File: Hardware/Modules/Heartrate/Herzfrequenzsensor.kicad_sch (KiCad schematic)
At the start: 8 parts, among them U1 MAX30101EFD_T, U2 TLV70018_SOT23-5, U4 PCA9306DCTR

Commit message: HeartRateV2
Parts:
- removed C3, C4: 1µ, Capacitor_SMD:C_0603_1608Metric_Pad1.08x0.95mm_HandSolder, symbol Device:C
- removed J1, J2: ~, Connector_JST:JST_EH_B4B-EH-A_1x04_P2.50mm_Vertical, symbol Modular_Electronics_Toolkit:CONN_I2C
- removed R1: 200k, Resistor_SMD:R_0603_1608Metric_Pad0.98x0.95mm_HandSolder, symbol Device:R
- removed U1: MAX30101EFD_T, Modular_Electronics_Toolkit:PSON80P560X330X165-14N, symbol Modular_Electronics_Toolkit:MAX30101EFD_T
- removed U2: TLV70018_SOT23-5, Package_TO_SOT_SMD:SOT-23-5, symbol Regulator_Linear:TLV70018_SOT23-5
- removed U4: PCA9306DCTR, Modular_Electronics_Toolkit:SOP65P400X130-8N, symbol Modular_Electronics_Toolkit:PCA9306DCTR
- added C10: 0.1µF, Capacitor_SMD:C_0603_1608Metric_Pad1.08x0.95mm_HandSolder, symbol Device:C
- added C11, C12: 4.7µF, Capacitor_SMD:C_0603_1608Metric_Pad1.08x0.95mm_HandSolder, symbol Device:C
- added C6, C7, C8, C9: 1µ, Capacitor_SMD:C_0603_1608Metric_Pad1.08x0.95mm_HandSolder, symbol Device:C
- added J4, J5: B4B-EH-A, Connector_JST:JST_EH_B4B-EH-A_1x04_P2.50mm_Vertical, symbol Modular_Electronics_Toolkit_sym:B4B-EH-A
- added J6: Conn_01x01_Pin, Connector_PinHeader_2.54mm:PinHeader_1x01_P2.54mm_Vertical, symbol Connector:Conn_01x01_Pin
- added R3: 200k, Resistor_SMD:R_0603_1608Metric_Pad0.98x0.95mm_HandSolder, symbol Device:R
- added R4, R5, R6, R7: 4.7k, Resistor_SMD:R_0603_1608Metric_Pad0.98x0.95mm_HandSolder, symbol Device:R
- added R8: 10R, Resistor_SMD:R_0603_1608Metric_Pad0.98x0.95mm_HandSolder, symbol Device:R
- added U6: MAX30101EFD_T, Modular_Electronics_Toolkit:PSON80P560X330X165-14N, symbol Modular_Electronics_Toolkit:MAX30101EFD_T
- added U7: PCA9306DCTR, Modular_Electronics_Toolkit:SOP65P400X130-8N, symbol Modular_Electronics_Toolkit:PCA9306DCTR
- added U8: MAX32664GTGA_T, Modular_Electronics_Toolkit:IC_MAX32664GTGA_T, symbol Modular_Electronics_Toolkit_sym:MAX32664GTGA_T
- added U9: TLV70018_SOT23-5, Package_TO_SOT_SMD:SOT-23-5, symbol Regulator_Linear:TLV70018_SOT23-5
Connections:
- net GND: now also C11.2, C12.2, C6.1, C7.1, C8.2, C9.2, J4.4, J5.4, R8.2, U6.12 (GND), U6.4 (PGND), U7.1 (GND), U8.10 (VSS__1), U8.7 (VSS), U9.2 (GND)
- new net: C6.2, U8.12 (VCORE)
- new net: C10.1, R8.1
- new net: R3.1, U7.7 (VREF2), U7.8 (EN)
- new net: C10.2, U8.6 (~{RST})
- new net B1: R4.1, U7.4 (SDA1), U8.23 (SLAVE_SDA)
- new net B2: R5.1, U7.3 (SCL1), U8.24 (SLAVE_SCL)
- new net B3: R6.1, U6.3 (SDA), U8.13 (SENSOR_SDA)
- new net B4: R7.1, U6.2 (SCL), U8.14 (SENSOR_SCL)
- new net INT: U6.13 (~{INT}), U8.18 (HR_INT)
- new net J1: J6.1 (Pin_1), U8.1 (MFIO)
- new net SCL: J4.2, J5.2, U7.6 (SCL2)
- new net SDA: J4.3, J5.3, U7.5 (SDA2)
- new net VCC: C11.1, C8.1, J4.1, J5.1, R3.2, U6.10 (VLED+__1), U6.9 (VLED+), U9.1 (IN)
- new net VDD__1: C7.2, C9.1, R4.2, R5.2, R6.2, R7.2, U8.11 (VDD), U8.22 (VDD__1), U9.5 (OUT)
- new net VREF: C12.1, U6.11 (VDD), U7.2 (VREF1)
- no-connect marks 0 -> 4

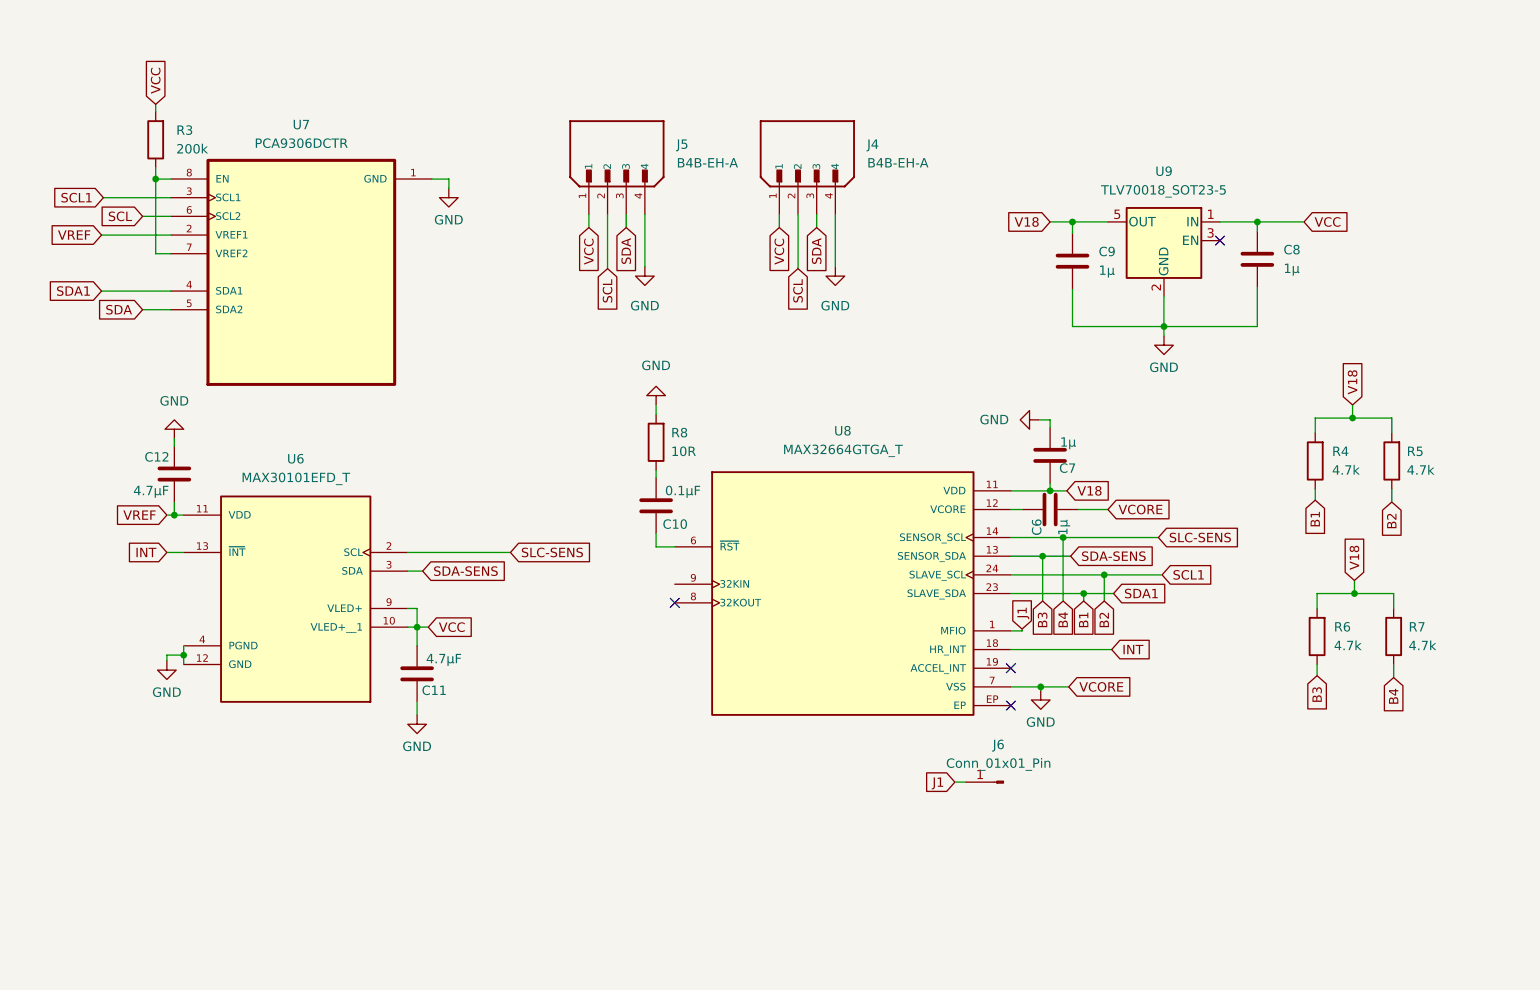
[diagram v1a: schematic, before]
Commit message: Finishing Modules
Wifi-Module
Flight-Module
REPAIR:
- Heartrate
- Flight-Module
- Wifi-Module
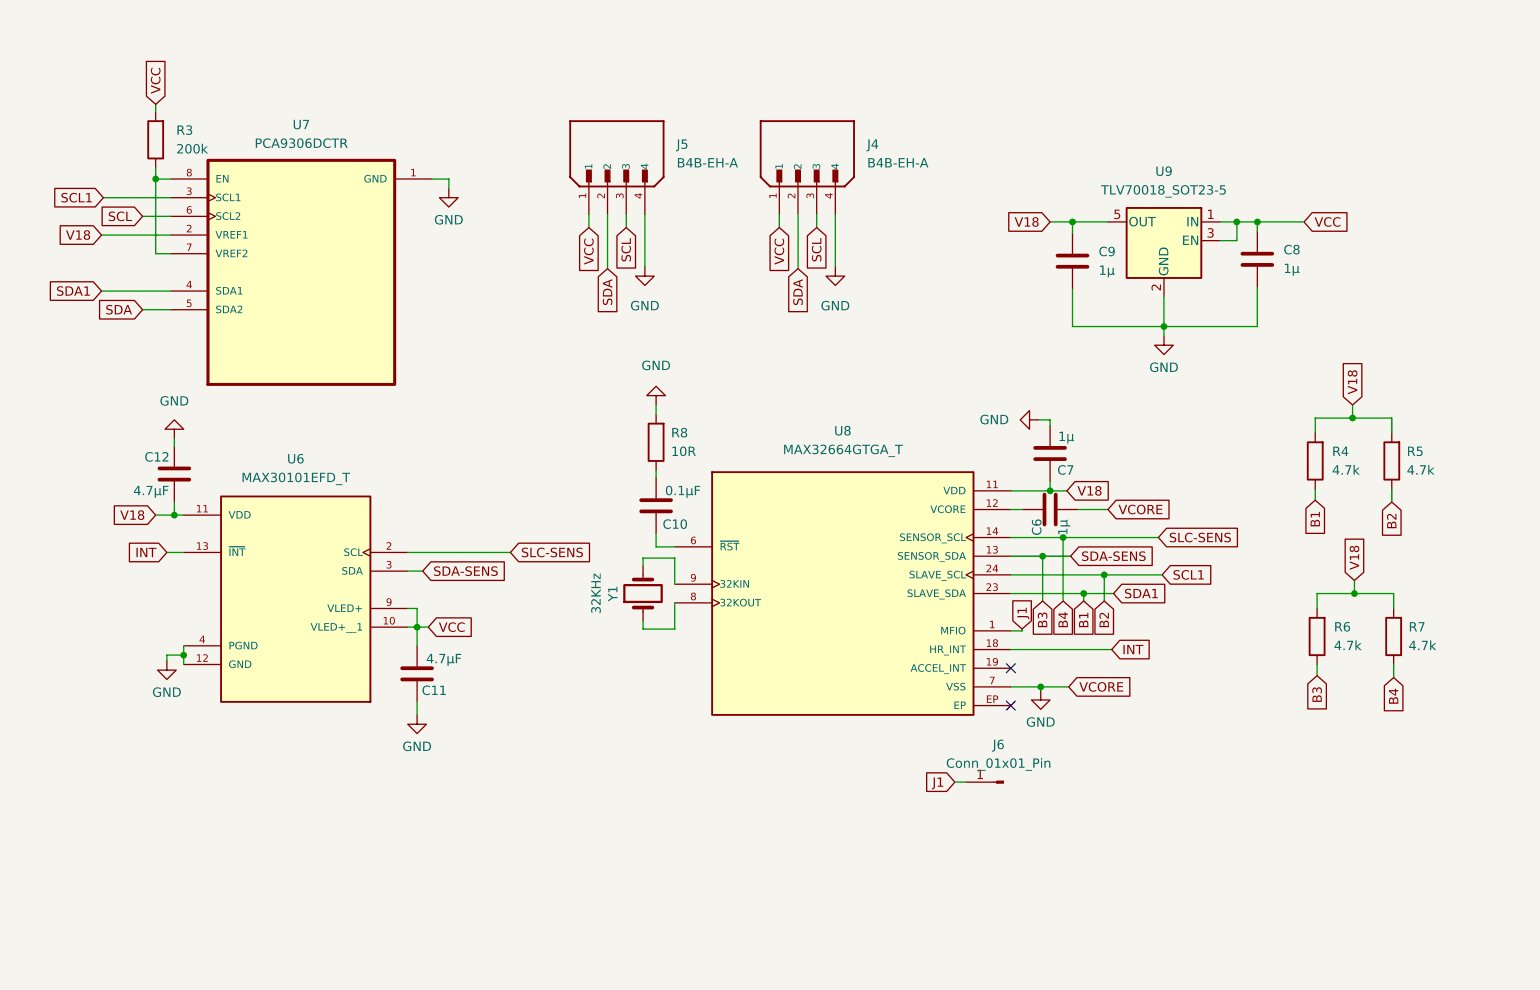
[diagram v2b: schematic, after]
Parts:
- added Y1: 32KHz, Modular-Electronics-Toolkit-BP:XTAL_CM7V-T1A-LOW-ESR-32.768KHZ-6PF-20-TA-QC, symbol Device:Crystal
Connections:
- net VREF is gone; now on net VDD__1: C12.1, U6.11 (VDD), U7.2 (VREF1)
- net SCL: now also J4.3, J5.3; no longer J4.2, J5.2
- net SDA: now also J4.2, J5.2; no longer J4.3, J5.3
- net VCC: now also U9.3 (EN)
- net at U8.8 (32KOUT): now also Y1.1
- net at U8.9 (32KIN): now also Y1.2
- no-connect marks 4 -> 2

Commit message: Pushing Final Versions of all Modules (2025)
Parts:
- Y1: footprint Modular-Electronics-Toolkit-BP:XTAL_CM7V-T1A-LOW-ESR-32.768KHZ-6PF-20-TA-QC -> Modular-Elektronics-Toolkit-Global-Libary:XTAL_CM7V-T1A-LOW-ESR-32.768KHZ-6PF-20-TA-QC
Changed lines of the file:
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@@
 (kicad_sch
-	(version 20231120)
+	(version 20250114)
 	(generator "eeschema")
-	(generator_version "8.0")
+	(generator_version "9.0")
 	(paper "A4")
 	(junction
@@
 	)
 	(junction
-		(at 162.052 107.188)
-		(diameter 0)
-		(color 0 0 0 0)
-	)
-	(junction
 		(at 45.466 102.87)
 		(diameter 0)
@@
 	(wire
 		(pts
-			(xy 162.052 107.188) (xy 165.862 107.188)
-		)
-		(stroke
-			(width 0)
-			(type default)
-		)
-	)
-	(wire
-		(pts
 			(xy 178.816 58.166) (xy 191.516 58.166)
 		)
@@
 		)
 	)
-	(global_label "VCORE"
-		(shape input)
-		(at 171.196 83.058 0)
-		(fields_autoplaced yes)
-		(effects
-			(font
-				(size 1.27 1.27)
-			)
-			(justify left)
-		)
-		(property "Intersheetrefs" "${INTERSHEET_REFS}"
-			(at 180.2893 83.058 0)
-			(effects
-				(font
-					(size 1.27 1.27)
-				)
-				(justify left)
-				(hide yes)
-			)
-		)
-	)
 	(global_label "SCL"
 		(shape input)
@@
 		)
 	)
-	(global_label "VCORE"
-		(shape input)
-		(at 165.862 107.188 0)
-		(fields_autoplaced yes)
-		(effects
-			(font
-				(size 1.27 1.27)
-			)
-			(justify left)
-		)
-		(property "Intersheetrefs" "${INTERSHEET_REFS}"
-			(at 174.9553 107.188 0)
-			(effects
-				(font
-					(size 1.27 1.27)
-				)
-				(justify left)
-				(hide yes)
-			)
-		)
-	)
 	(global_label "VCC"
 		(shape input)
@@
 			)
 		)
-		(property "Footprint" "Modular-Electronics-Toolkit-BP:XTAL_CM7V-T1A-LOW-ESR-32.768KHZ-6PF-20-TA-QC"
+		(property "Footprint" "Modular-Elektronics-Toolkit-Global-Libary:XTAL_CM7V-T1A-LOW-ESR-32.768KHZ-6PF-20-TA-QC"
 			(at 107.95 94.488 0)
 			(effects
@@
 	(symbol
 		(lib_id "power:GND")
+		(at 171.196 83.058 90)
+		(unit 1)
+		(exclude_from_sim no)
+		(in_bom yes)
+		(on_board yes)
+		(dnp no)
+		(fields_autoplaced yes)
+		(property "Reference" "#PWR010"
+			(at 177.546 83.058 0)
+			(effects
+				(font
+					(size 1.27 1.27)
+				)
+				(hide yes)
+			)
+		)
+		(property "Value" "GND"
+			(at 174.498 83.0579 90)
+			(effects
+				(font
+					(size 1.27 1.27)
+				)
+				(justify right)
+			)
+		)
+		(property "Footprint" ""
+			(at 171.196 83.058 0)
+			(effects
+				(font
+					(size 1.27 1.27)
+				)
+				(hide yes)
+			)
+		)
+		(property "Datasheet" ""
+			(at 171.196 83.058 0)
+			(effects
+				(font
+					(size 1.27 1.27)
+				)
+				(hide yes)
+			)
+		)
+		(property "Description" "Power symbol creates a global label with name \"GND\" , ground"
+			(at 171.196 83.058 0)
+			(effects
+				(font
+					(size 1.27 1.27)
+				)
+				(hide yes)
+			)
+		)
+		(pin "1"
+		)
+		(instances
+			(project "Herzfrequenzsensor"
+				(path "/75650d24-5baf-445f-b391-8e8a09b0afdd"
+					(reference "#PWR010")
+					(unit 1)
+				)
+			)
+		)
+	)
+	(symbol
+		(lib_id "power:GND")
 		(at 81.534 39.37 0)
 		(unit 1)
@@
 		)
 	)
+	(embedded_fonts no)
 )

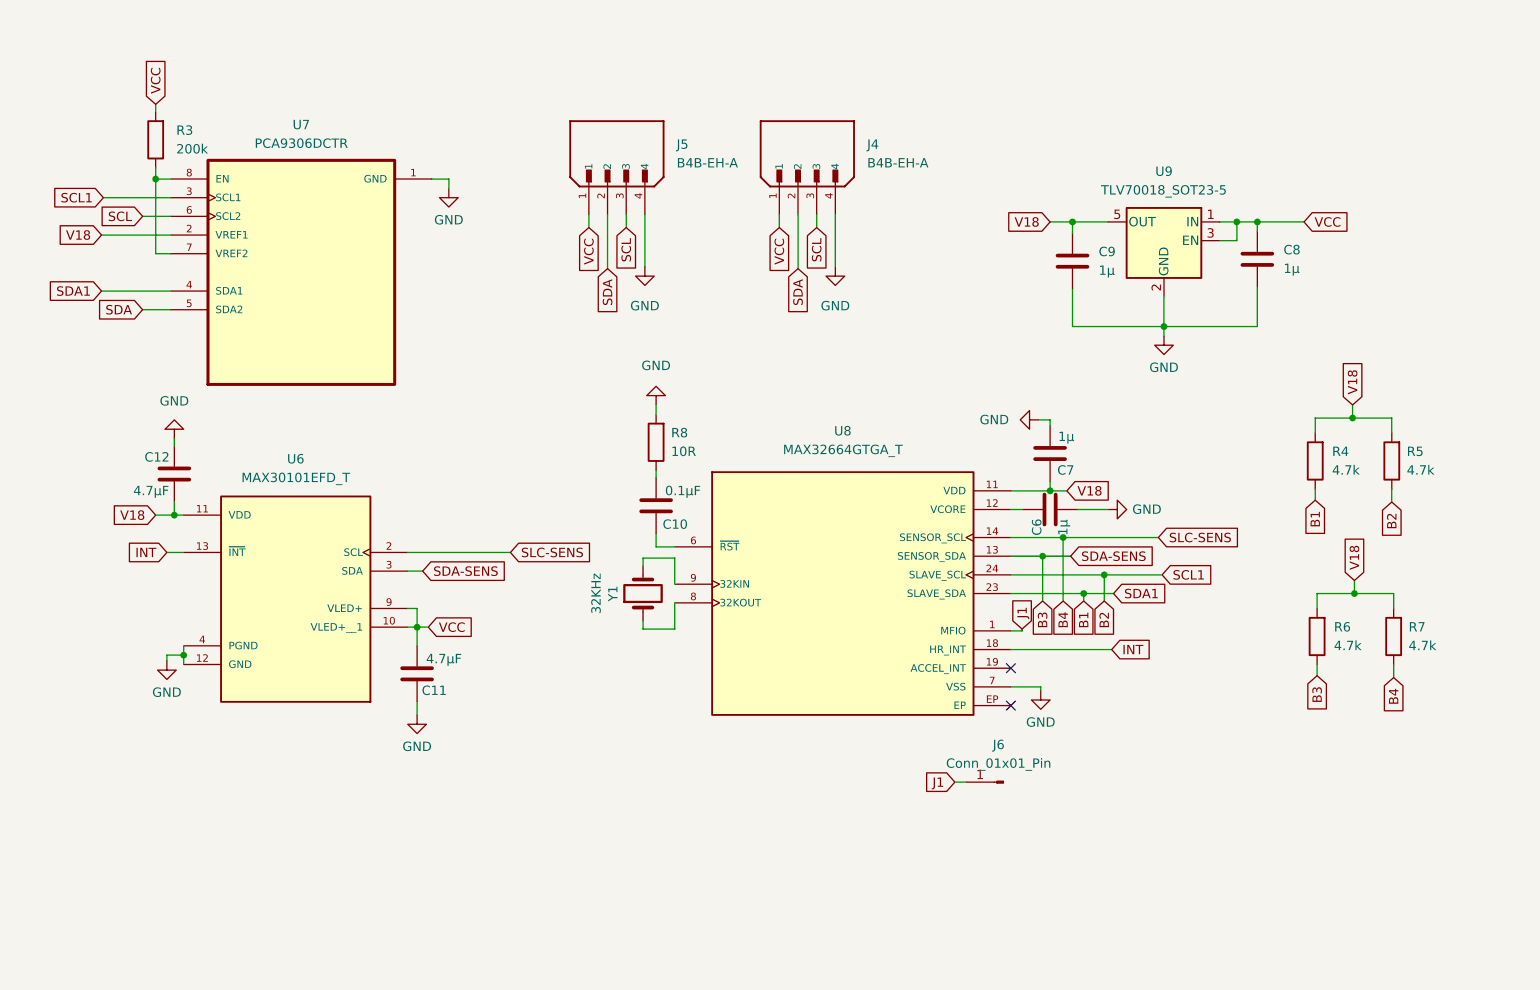
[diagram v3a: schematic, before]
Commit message: Finall Version of the Wifi-Module (correct mistakes))
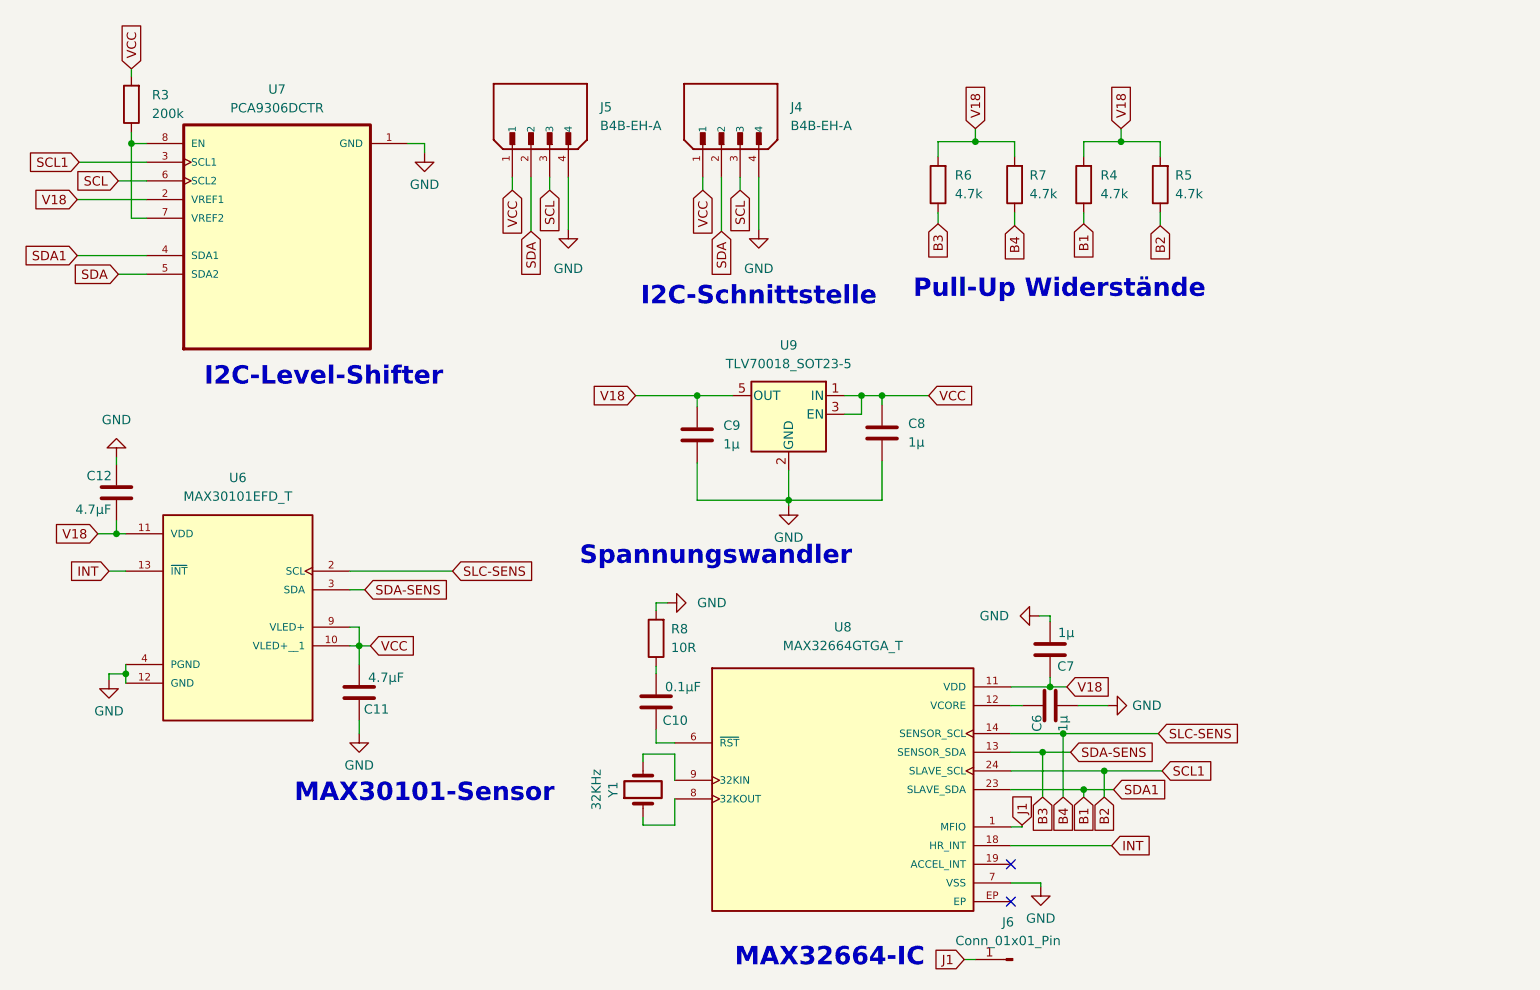
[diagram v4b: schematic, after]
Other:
- note added: "I2C-Level-Shifter"
- note added: "I2C-Schnittstelle"
- note added: "MAX30101-Sensor"
- note added: "MAX32664-IC"
- note added: "Pull-Up Widerstände"
- note added: "Spannungswandler"
- moved on the sheet: C10, C11, C12, C6, C7, C8, C9, J4, J5, J6, R3, R4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
